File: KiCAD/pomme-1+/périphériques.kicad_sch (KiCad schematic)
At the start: 23 parts, among them J4 rs232-socket, J5 rs232-plug, J6 5V MCU UART, J7 DE9_female, Q1 2N3904, U10 MAX232CPE

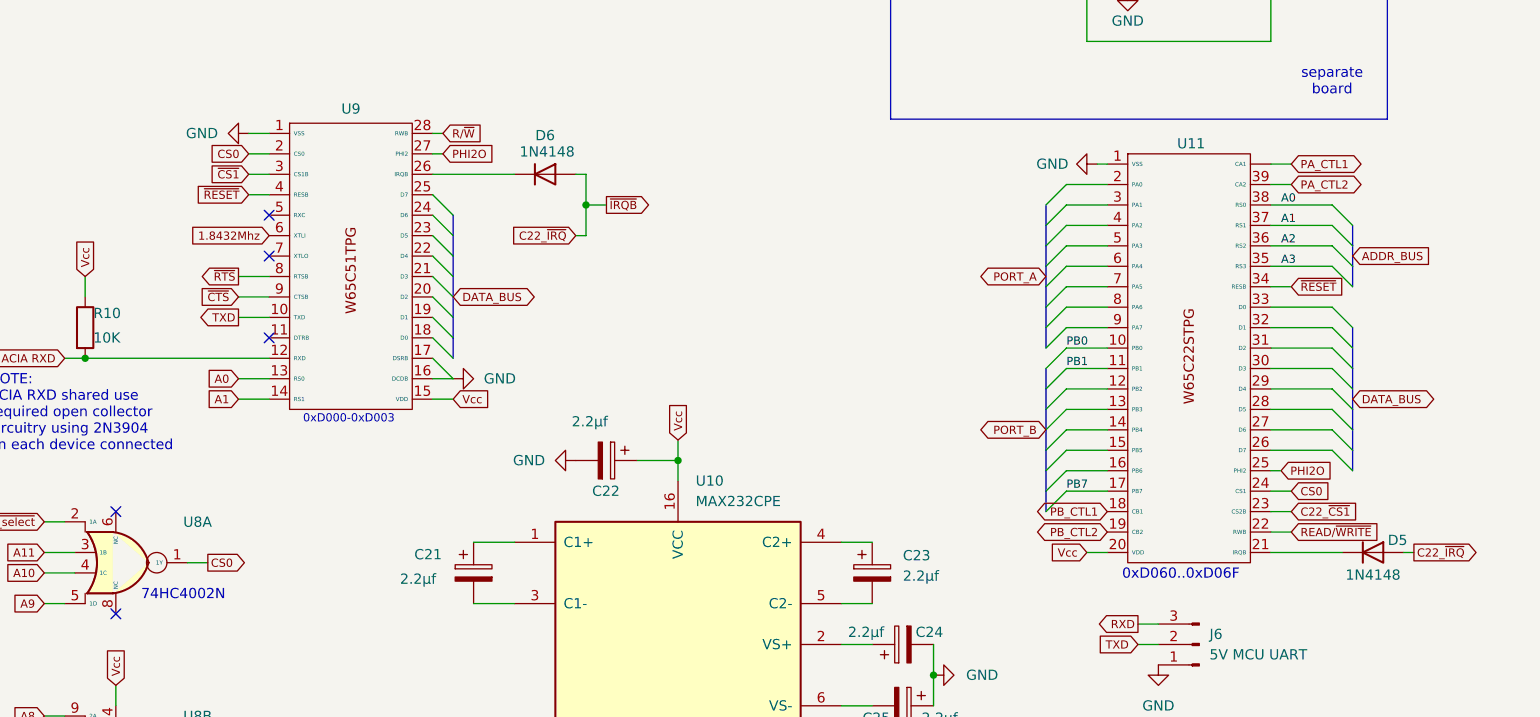
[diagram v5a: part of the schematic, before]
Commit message: Modification schématique V1.5
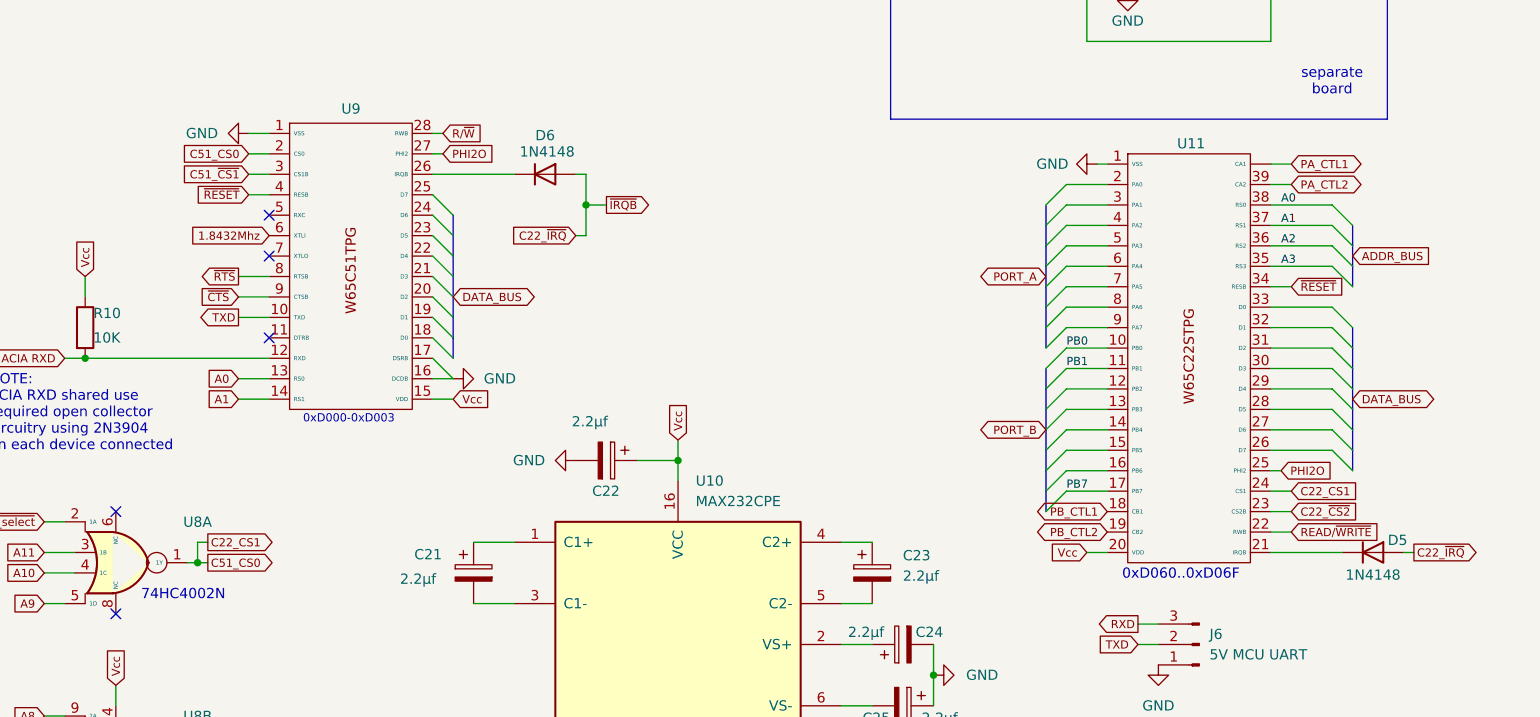
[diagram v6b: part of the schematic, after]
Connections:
- net C22_~{CS1} renamed C22_~{CS2}
- net CS0 renamed C22_CS1
- net ~{CS1} renamed C51_~{CS1}
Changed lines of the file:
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@@
 	)
 	(junction
+		(at 106.68 104.14)
+		(diameter 0)
+		(color 0 0 0 0)
+	)
+	(junction
 		(at 78.74 161.29)
 		(diameter 0)
@@
 	(wire
 		(pts
+			(xy 106.68 104.14) (xy 107.95 104.14)
+		)
+		(stroke
+			(width 0)
+			(type default)
+		)
+	)
+	(wire
+		(pts
 			(xy 218.44 54.61) (xy 219.71 54.61)
 		)
@@
 	(wire
 		(pts
+			(xy 106.68 101.6) (xy 106.68 104.14)
+		)
+		(stroke
+			(width 0)
+			(type default)
+		)
+	)
+	(wire
+		(pts
 			(xy 240.03 95.25) (xy 242.57 95.25)
 		)
@@
 	(wire
 		(pts
+			(xy 107.95 101.6) (xy 106.68 101.6)
+		)
+		(stroke
+			(width 0)
+			(type default)
+		)
+	)
+	(wire
+		(pts
 			(xy 223.52 111.76) (xy 226.06 111.76)
 		)
@@
 	(wire
 		(pts
-			(xy 105.41 104.14) (xy 107.95 104.14)
+			(xy 105.41 104.14) (xy 106.68 104.14)
 		)
 		(stroke
@@
 		)
 	)
-	(global_label "CS0"
+	(global_label "C51_CS0"
 		(shape output)
 		(at 107.95 104.14 0)
@@
 		)
 		(property "Intersheetrefs" "${INTERSHEET_REFS}"
-			(at 113.2891 104.14 0)
+			(at 117.0144 104.14 0)
 			(effects
 				(font
@@
 		)
 	)
-	(global_label "~{CS1}"
+	(global_label "C51_~{CS1}"
 		(shape input)
 		(at 113.03 55.88 180)
@@
 		)
 		(property "Intersheetrefs" "${INTERSHEET_REFS}"
-			(at 107.6909 55.88 0)
+			(at 103.9656 55.88 0)
 			(effects
 				(font
@@
 		)
 	)
-	(global_label "C22_~{CS1}"
+	(global_label "C22_~{CS2}"
 		(shape input)
 		(at 242.57 97.79 0)
@@
 		)
 	)
-	(global_label "CS0"
+	(global_label "C22_CS1"
 		(shape input)
 		(at 242.57 95.25 0)
@@
 		)
 		(property "Intersheetrefs" "${INTERSHEET_REFS}"
-			(at 247.9091 95.25 0)
+			(at 251.6344 95.25 0)
 			(effects
 				(font
@@
 		)
 	)
+	(global_label "C22_CS1"
+		(shape output)
+		(at 107.95 101.6 0)
+		(fields_autoplaced yes)
+		(effects
+			(font
+				(size 1.016 1.016)
+			)
+			(justify left)
+		)
+		(property "Intersheetrefs" "${INTERSHEET_REFS}"
+			(at 117.0144 101.6 0)
+			(effects
+				(font
+					(size 1.27 1.27)
+				)
+				(justify left)
+				(hide yes)
+			)
+		)
+	)
 	(global_label "CB1"
 		(shape input)
@@
 		)
 	)
-	(global_label "CS0"
+	(global_label "C51_CS0"
 		(shape input)
 		(at 113.03 53.34 180)
@@
 		)
 		(property "Intersheetrefs" "${INTERSHEET_REFS}"
-			(at 107.6909 53.34 0)
+			(at 103.9656 53.34 0)
 			(effects
 				(font

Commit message: Modification circuit périphériques
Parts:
- removed R12: 2K2, symbol Device:R
- added J3: RTS|CTS loop, symbol Connector:Conn_01x02_Pin
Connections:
- net rs232-cts: now also J3.2 (Pin_2)
- net rs232-rts: now also J3.1 (Pin_1)
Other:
- note added: "close for no hard flow control"
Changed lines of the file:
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@@
 	)
 	(junction
+		(at 194.31 142.24)
+		(diameter 0)
+		(color 0 0 0 0)
+	)
+	(junction
 		(at 201.93 137.16)
 		(diameter 0)
@@
 	)
 	(junction
+		(at 191.77 132.08)
+		(diameter 0)
+		(color 0 0 0 0)
+	)
+	(junction
 		(at 154.94 59.69)
 		(diameter 0)
@@
 		(color 0 0 0 0)
 	)
-	(junction
-		(at 186.69 142.24)
-		(diameter 0)
-		(color 0 0 0 0)
-	)
 	(no_connect
 		(at 234.95 157.48)
@@
 		)
 	)
+	(wire
+		(pts
+			(xy 194.31 142.24) (xy 199.39 142.24)
+		)
+		(stroke
+			(width 0)
+			(type default)
+		)
+	)
 	(bus
 		(pts
@@
 	(wire
 		(pts
-			(xy 186.69 142.24) (xy 199.39 142.24)
+			(xy 186.69 142.24) (xy 194.31 142.24)
 		)
 		(stroke
@@
 	(wire
 		(pts
+			(xy 194.31 142.24) (xy 194.31 151.13)
+		)
+		(stroke
+			(width 0)
+			(type default)
+		)
+	)
+	(wire
+		(pts
 			(xy 135.89 50.8) (xy 137.16 50.8)
 		)
@@
 	(wire
 		(pts
-			(xy 186.69 132.08) (xy 204.47 132.08)
+			(xy 191.77 132.08) (xy 191.77 151.13)
+		)
+		(stroke
+			(width 0)
+			(type default)
+		)
+	)
+	(wire
+		(pts
+			(xy 186.69 132.08) (xy 191.77 132.08)
 		)
 		(stroke
@@
 	(wire
 		(pts
+			(xy 191.77 132.08) (xy 204.47 132.08)
+		)
+		(stroke
+			(width 0)
+			(type default)
+		)
+	)
+	(wire
+		(pts
 			(xy 240.03 30.48) (xy 243.84 30.48)
 		)
@@
 		)
 	)
+	(text "close\nfor no hard flow\ncontrol"
+		(exclude_from_sim no)
+		(at 193.294 159.258 0)
+		(effects
+			(font
+				(size 1.016 1.016)
+			)
+		)
+	)
 	(text "To terminal"
 		(exclude_from_sim no)
@@
 		)
 	)
-	(global_label "Vcc"
-		(shape input)
-		(at 186.69 149.86 270)
-		(fields_autoplaced yes)
-		(effects
-			(font
-				(size 1.016 1.016)
-			)
-			(justify right)
-		)
-		(property "Intersheetrefs" "${INTERSHEET_REFS}"
-			(at 186.69 154.8606 90)
-			(effects
-				(font
-					(size 1.27 1.27)
-				)
-				(justify right)
-				(hide yes)
-			)
-		)
-	)
 	(global_label "C22_~{IRQ}"
 		(shape output)
@@
 	)
 	(symbol
+		(lib_id "Connector:Conn_01x02_Pin")
+		(at 191.77 156.21 90)
+		(unit 1)
+		(exclude_from_sim no)
+		(in_bom yes)
+		(on_board yes)
+		(dnp no)
+		(property "Reference" "J3"
+			(at 195.58 154.3049 90)
+			(effects
+				(font
+					(size 1.27 1.27)
+				)
+				(justify right)
+			)
+		)
+		(property "Value" "RTS|CTS loop"
+			(at 180.34 154.94 90)
+			(effects
+				(font
+					(size 1.016 1.016)
+				)
+				(justify right)
+			)
+		)
+		(property "Footprint" ""
+			(at 191.77 156.21 0)
+			(effects
+				(font
+					(size 1.27 1.27)
+				)
+				(hide yes)
+			)
+		)
+		(property "Datasheet" "~"
+			(at 191.77 156.21 0)
+			(effects
+				(font
+					(size 1.27 1.27)
+				)
+				(hide yes)
+			)
+		)
+		(property "Description" "Generic connector, single row, 01x02, script generated"
+			(at 191.77 156.21 0)
+			(effects
+				(font
+					(size 1.27 1.27)
+				)
+				(hide yes)
+			)
+		)
+		(pin "1"
+		)
+		(pin "2"
+		)
+		(instances
+			(project ""
+				(path "/46a37b86-f1f5-4cd9-9809-f219c84ab6f2/b95291a5-dff0-4cc1-8588-7d50061f5092"
+					(reference "J3")
+					(unit 1)
+				)
+			)
+		)
+	)
+	(symbol
 		(lib_id "power:GND")
 		(at 222.25 33.02 0)
@@
 				)
 			)
-		)
-	)
-	(symbol
-		(lib_id "Device:R")
-		(at 186.69 146.05 180)
-		(unit 1)
-		(exclude_from_sim no)
-		(in_bom yes)
-		(on_board yes)
-		(dnp no)
-		(property "Reference" "R12"
-			(at 188.468 147.574 0)
-			(effects
-				(font
-					(size 1.27 1.27)
-				)
-				(justify right)
-			)
-		)
-		(property "Value" "2K2"
-			(at 186.69 148.082 90)
-			(effects
-				(font
-					(size 1.27 1.27)
-				)
-				(justify right)
-			)
-		)
-		(property "Footprint" ""
-			(at 188.468 146.05 90)
-			(effects
-				(font
-					(size 1.27 1.27)
-				)
-				(hide yes)
-			)
-		)
-		(property "Datasheet" "~"
-			(at 186.69 146.05 0)
-			(effects
-				(font
-					(size 1.27 1.27)
-				)
-				(hide yes)
-			)
-		)
-		(property "Description" "Resistor"
-			(at 186.69 146.05 0)
-			(effects
-				(font
-					(size 1.27 1.27)
-				)
-				(hide yes)
-			)
-		)
-		(pin "2"
-		)
-		(pin "1"
-		)
-		(instances
-			(project ""
-				(path "/46a37b86-f1f5-4cd9-9809-f219c84ab6f2/b95291a5-dff0-4cc1-8588-7d50061f5092"
-					(reference "R12")
-					(unit 1)
-				)
-			)

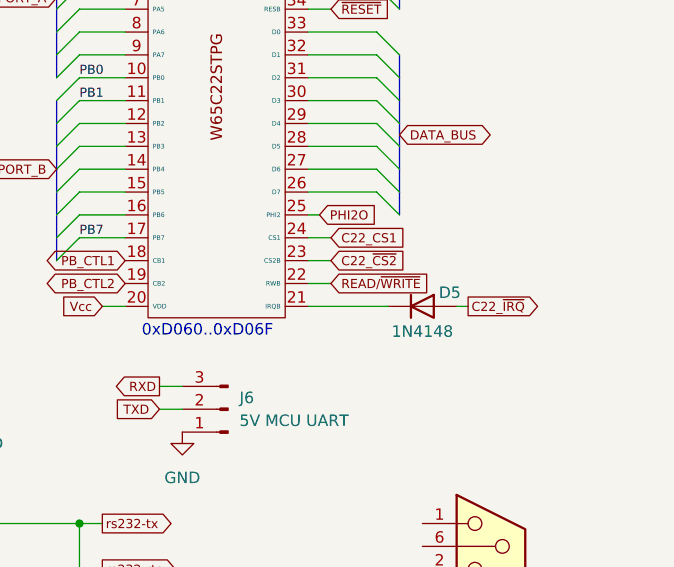
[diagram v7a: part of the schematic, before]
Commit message: Correction à la schématique les W65C51S et W65C22S doivent revevoir le signal RWB du mpu plutôt que le signal READ/WRITEB à la pin 8 de U3
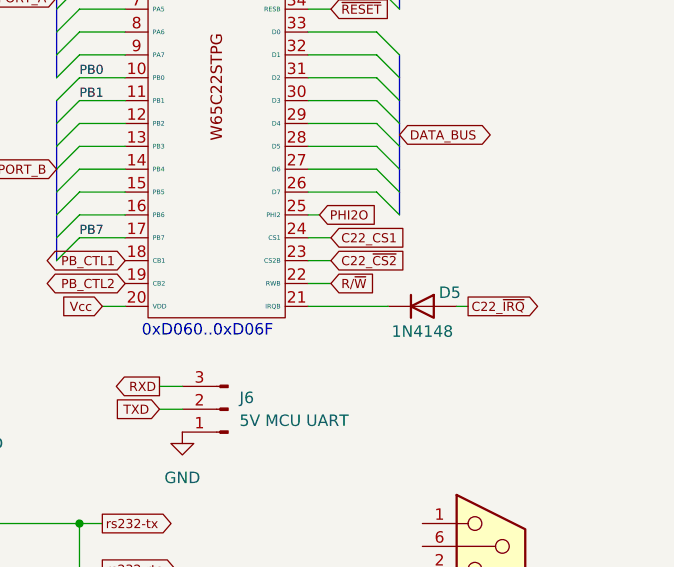
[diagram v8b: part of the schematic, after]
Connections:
- net READ/~{WRITE} is gone; now on net R/~{W}: U11.22 (RWB)
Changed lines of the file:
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@@
 		)
 	)
-	(global_label "READ{slash}~{WRITE}"
+	(global_label "R{slash}~{W}"
 		(shape input)
 		(at 242.57 100.33 0)
@@
 		)
 		(property "Intersheetrefs" "${INTERSHEET_REFS}"
-			(at 254.1986 100.33 0)
+			(at 248.1994 100.33 0)
 			(effects
 				(font
